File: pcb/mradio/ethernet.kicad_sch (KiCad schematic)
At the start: 28 parts, among them J1 JX0026D21BNL, U2 DP83825I, Y301 DSC1525JL2A-25M00000T

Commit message: ethernet oscillator
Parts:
- added C301: 0.01uF, symbol Device:C_Small
- added Q301: DN2540N3-G, Package_TO_SOT_THT:TO-92_Inline, symbol Transistor_FET_Other:DN2540N3-G
- renumbered C301 to C302, C4 to C303, C3 to C304, C2 to C305, C1 to C306, C8 to C307, C7 to C308, C6 to C309, C5 to C310, C313 to C311, C314 to C312, FB1 to FB301, FB2 to FB302, J1 to J301, R1 to R302, TP302 to TP301, TP303 to TP302, TP4 to TP303, TP3 to TP304, TP1 to TP305, TP2 to TP306, TP301 to TP307, U2 to U301
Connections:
- net +1V8: now also C302.1, Y301.4 (Vcc)
- net ETH_MDIO: now also U301.15 (MDIO)
- net ETH_RESET: now also Q301.2 (G); no longer TP302.1, U301.5 (~{RST})
- net GND: now also Y301.2 (GND), C301.2
- net at R302.2: now also Y301.1 (OE)
- net at TP301.1, U301.13 (XI/50MHzIn): now also Y301.3 (OUT)
- net at R301.1: now also Q301.1 (S)
- new net: C301.1, Q301.3 (D), TP302.1, U301.5 (~{RST})
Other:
- moved on the sheet: C302, R303, Y301

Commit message: Fixed numbers
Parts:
- removed C301: 0.01uF, symbol Device:C_Small
- removed C312: 0.1uF, symbol Device:C_Small
- removed J301: JX0026D21BNL, JX0026D21BNL:JX0026D21BNL, symbol symbols:JX0026D21BNL
- removed Q301: DN2540N3-G, Package_TO_SOT_THT:TO-92_Inline, symbol Transistor_FET_Other:DN2540N3-G
- removed R301: 2.2k, Package_TO_SOT_THT:TO-92_Inline, symbol Device:R
- removed R302: 70k, symbol Device:R_Small
- removed R305: R, symbol Device:R
- removed TP301, TP302, TP303, TP304, TP305, TP306, TP307: TestPoint, symbol Connector:TestPoint
- added C309: 0.1uF, symbol Device:C_Small
- added J301: RJ45_Wuerth_7499010211A, Connector_RJ:RJ45_Wuerth_7499010211A_Horizontal, symbol Connector:RJ45_Wuerth_7499010211A
- added R303: R, symbol Device:R
- R301: renamed from R303; value 2.2k -> (none)
- renumbered C302 to C301, C303 to C302, C304 to C303, C305 to C304, C306 to C305, C307 to C306, C308 to C307, C309 to C308, R304 to R302
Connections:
- net +1V8: now also Y301.1 (OE)
- net ETH_LINK: now also R303.2
- net ETH_RESET: now also U301.5 (~{RST})
- net GND: now also C309.2, J301.10, J301.11, J301.12
- net at U301.11 (TD+): now also J301.1 (TD+)
- net at U301.10 (TD-): now also J301.2 (TD-)
- net at C311.2: now also J301.4 (CTD)
- net at U301.8 (RD+): now also J301.3 (RD+)
- net at U301.7 (RD-): now also J301.6 (RD-)
- new net: C309.1, J301.5 (CRD)
- new net: J301.9, R303.1
- new net GNDPWR: J301.SH
- no-connect marks 6 -> 2
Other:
- moved on the sheet: C301, R301, R302, Y301

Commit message: undid overwrite
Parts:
- removed C309: 0.1uF, symbol Device:C_Small
- removed J301: RJ45_Wuerth_7499010211A, Connector_RJ:RJ45_Wuerth_7499010211A_Horizontal, symbol Connector:RJ45_Wuerth_7499010211A
- removed R303: R, symbol Device:R
- added C301: 0.01uF, symbol Device:C_Small
- added C312: 0.1uF, symbol Device:C_Small
- added J301: JX0026D21BNL, JX0026D21BNL:JX0026D21BNL, symbol symbols:JX0026D21BNL
- added Q301: DN2540N3-G, Package_TO_SOT_THT:TO-92_Inline, symbol Transistor_FET_Other:DN2540N3-G
- added R301: 2.2k, Package_TO_SOT_THT:TO-92_Inline, symbol Device:R
- added R302: 70k, symbol Device:R_Small
- added R305: R, symbol Device:R
- added TP301, TP302, TP303, TP304, TP305, TP306, TP307: TestPoint, symbol Connector:TestPoint
- R303: renamed from R301; value (none) -> 2.2k
- renumbered C301 to C302, C302 to C303, C303 to C304, C304 to C305, C305 to C306, C306 to C307, C307 to C308, C308 to C309, R302 to R304
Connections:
- net +1V8: now also R302.1; no longer Y301.1 (OE)
- net ETH_LINK: now also R305.2
- net ETH_RESET: now also Q301.2 (G); no longer U301.5 (~{RST})
- net ETH_RXD0: now also TP303.1
- net ETH_RXD1: now also TP304.1
- net ETH_TXD0: now also TP305.1
- net ETH_TXD1: now also TP306.1
- net GND: now also C301.2, C312.1, J301.12 (A_GREEN), J301.4 (CHS_GROUND_1), J301.5 (CHS_GROUND_2), R301.2
- net at U301.11 (TD+): now also J301.1 (TD+)
- net at U301.10 (TD-): now also J301.2 (TD-)
- net at U301.8 (RD+): now also J301.7 (RD+)
- net at C311.2: now also J301.3 (CT_1)
- net at U301.7 (RD-): now also J301.8 (RD-)
- net at U301.13 (XI/50MHzIn), Y301.3 (OUT): now also TP301.1
- net at R304.1, U301.14 (RBIAS): now also TP307.1
- new net: Q301.1 (S), R301.1
- new net: C301.1, Q301.3 (D), TP302.1, U301.5 (~{RST})
- new net: R302.2, Y301.1 (OE)
- new net: J301.11 (K_GREEN), R305.1
- new net: C312.2, J301.6 (CT_2)
- no-connect marks 2 -> 6
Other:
- moved on the sheet: C302, R303, R304, Y301

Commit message: ethernet erc
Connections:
- net ETH_LINK: now also U301.16 (MDC); no longer U301.4 (LED0/S(ANEG_Dis))
- net ETH_MDC: now also U301.4 (LED0/S(ANEG_Dis)); no longer U301.16 (MDC)

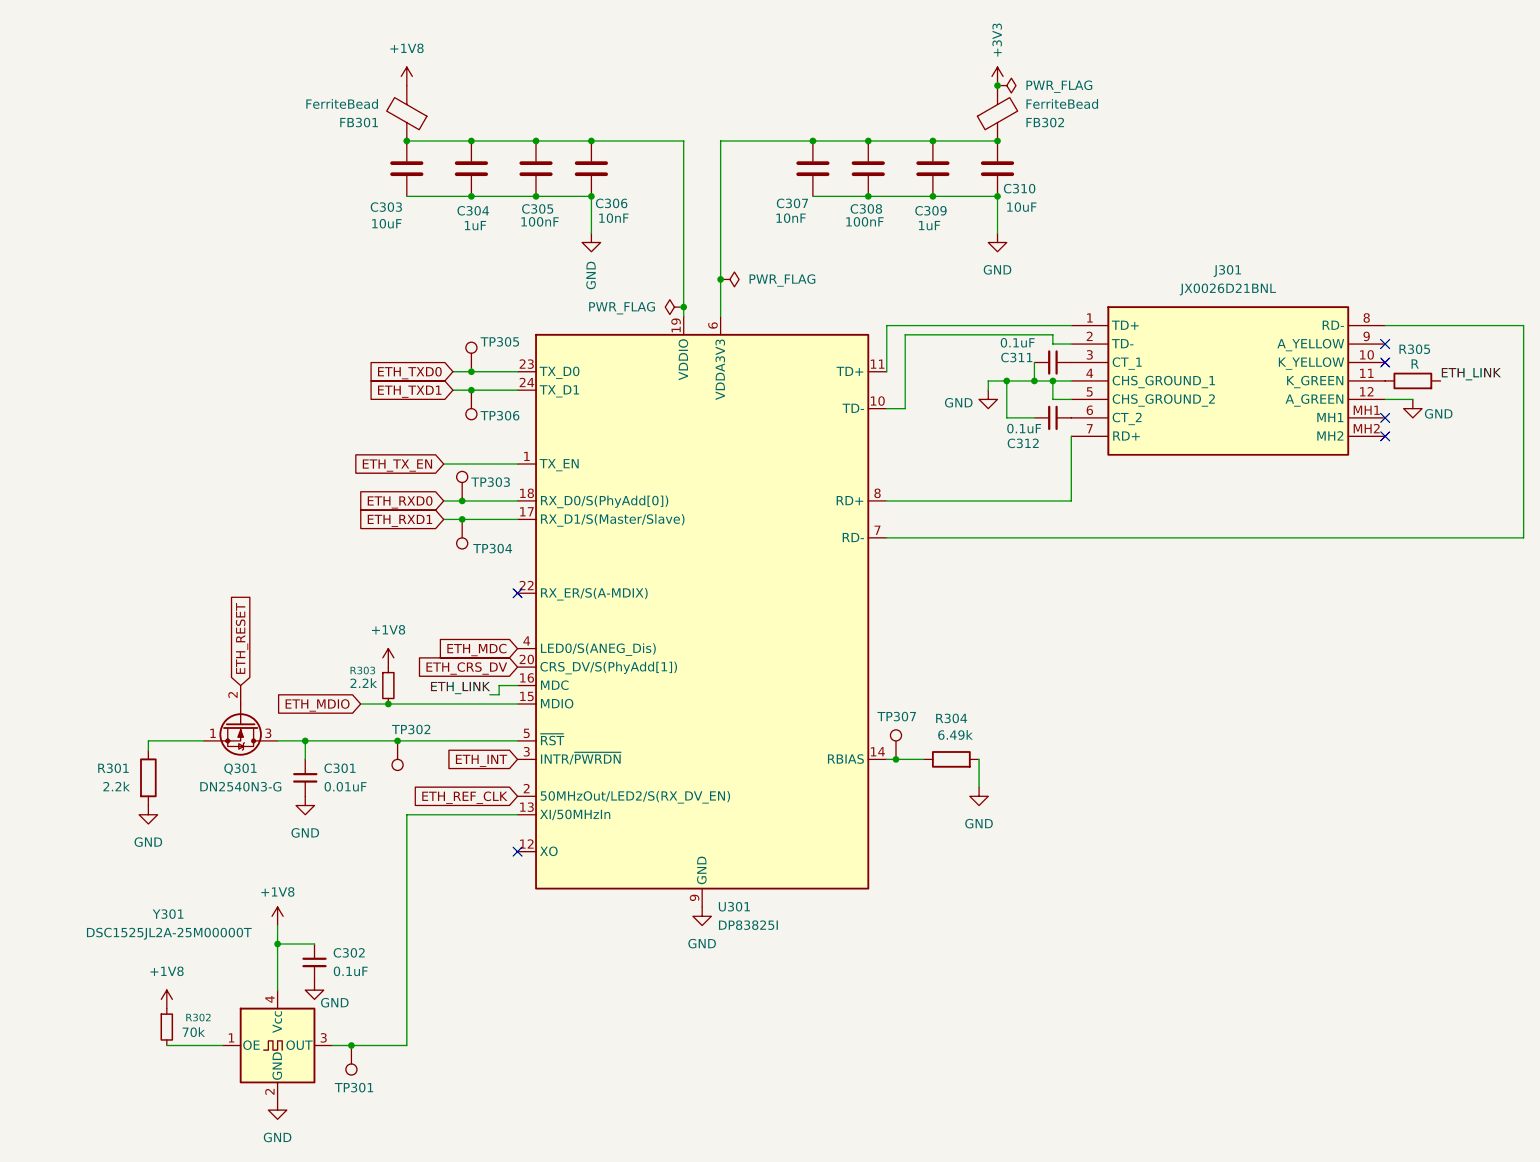
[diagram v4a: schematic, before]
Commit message: changed eth mosfet
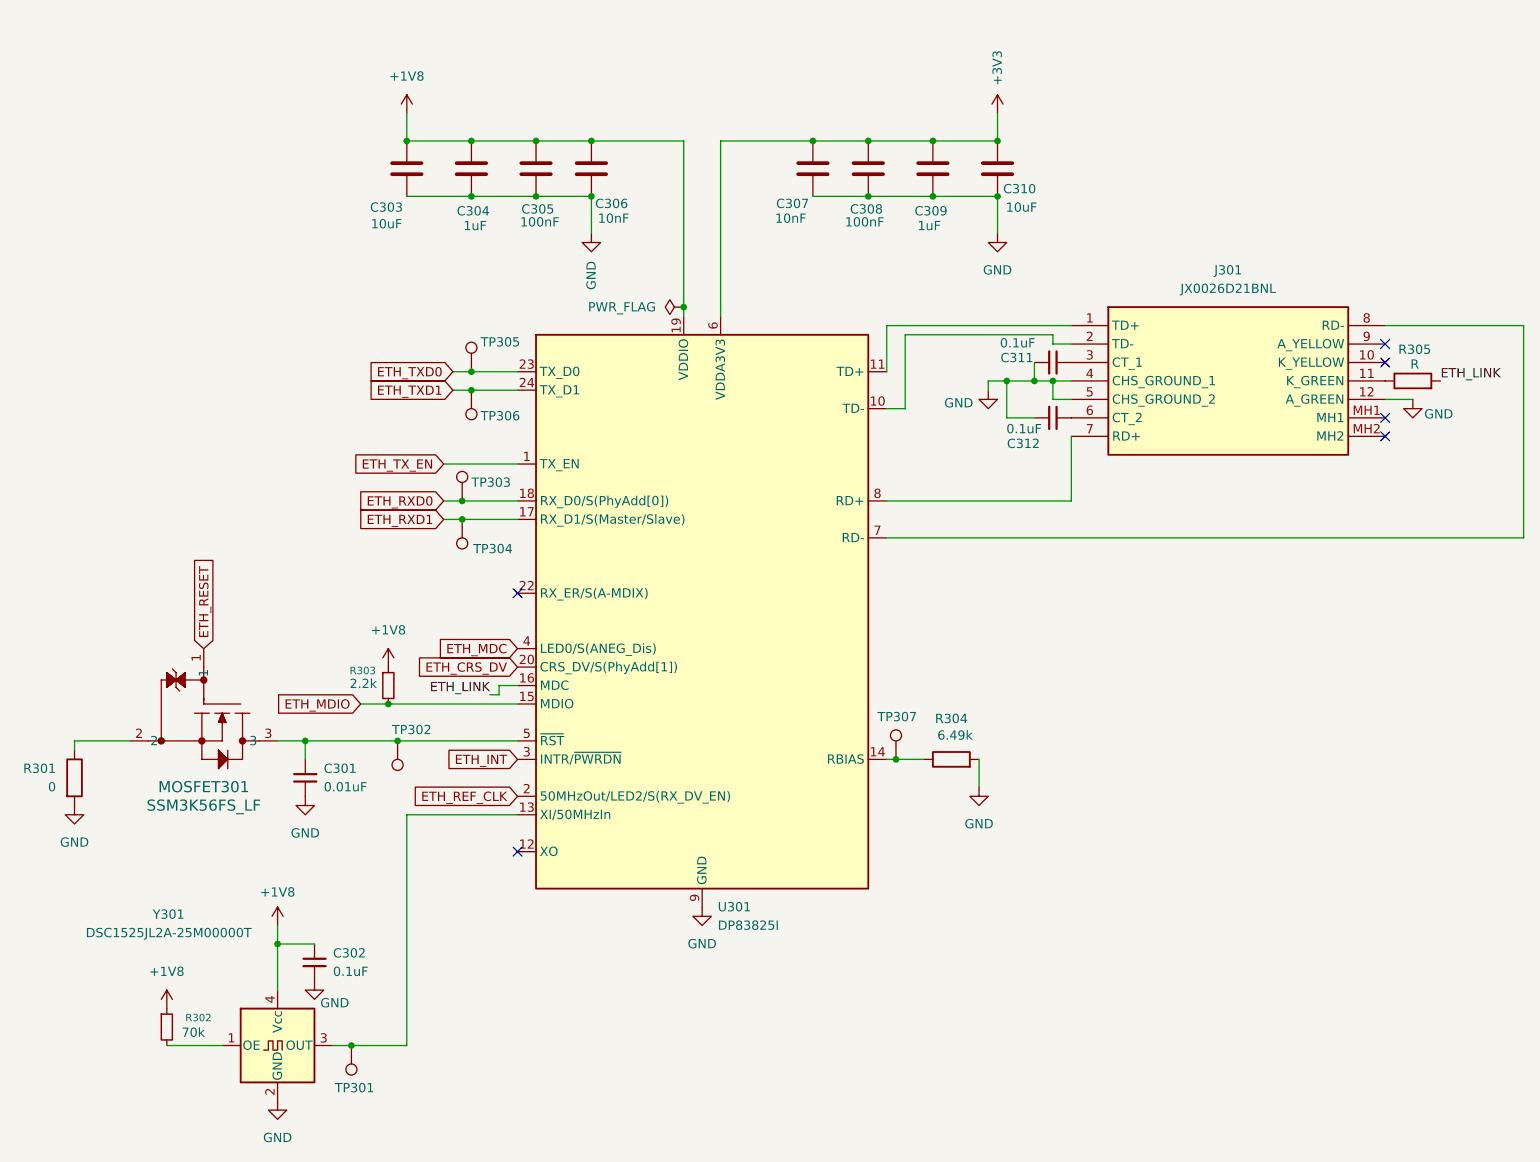
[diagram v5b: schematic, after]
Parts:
- removed FB301, FB302: FerriteBead, Package_LCC:PLCC-84_29.3x29.3mm_P1.27mm, symbol Device:FerriteBead
- removed Q301: DN2540N3-G, Package_TO_SOT_THT:TO-92_Inline, symbol Transistor_FET_Other:DN2540N3-G
- added MOSFET301: SSM3K56FS_LF, SSM3K56FS:SSM_TOS, symbol symbols:SSM3K56FS_LF
- C301, C302, C303, C304, C305, C308, C309, C310, C311, C312: footprint (none) -> Capacitor_SMD:C_0603_1608Metric
- C306, C307: footprint Package_SO:SOIC-8_3.9x4.9mm_P1.27mm -> Capacitor_SMD:C_0603_1608Metric
- R301: value 2.2k -> 0; footprint Package_TO_SOT_THT:TO-92_Inline -> Resistor_SMD:R_0603_1608Metric
- R302, R303, R304, R305: footprint (none) -> Resistor_SMD:R_0603_1608Metric
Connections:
- net +1V8: now also C303.2, C304.2, C305.2, C306.2, U301.19 (VDDIO)
- net +3V3: now also C307.2, C308.2, C309.2, C310.2, U301.6 (VDDA3V3)
- net ETH_RESET: now also MOSFET301.1
- net at R301.1: now also MOSFET301.2
- net at C301.1, TP302.1, U301.5 (~{RST}): now also MOSFET301.3
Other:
- moved on the sheet: R301

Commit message: Update some footprints
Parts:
- TP301, TP302, TP303, TP304, TP305, TP306, TP307: footprint (none) -> TestPoint:TestPoint_Loop_D2.60mm_Drill0.9mm_Beaded
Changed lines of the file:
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@@
 			)
 		)
-		(property "Footprint" ""
+		(property "Footprint" "TestPoint:TestPoint_Loop_D2.60mm_Drill0.9mm_Beaded"
 			(at 90.17 171.45 0)
 			(hide yes)
@@
 			)
 		)
-		(property "Footprint" ""
+		(property "Footprint" "TestPoint:TestPoint_Loop_D2.60mm_Drill0.9mm_Beaded"
 			(at 115.57 96.52 0)
 			(hide yes)
@@
 			)
 		)
-		(property "Footprint" ""
+		(property "Footprint" "TestPoint:TestPoint_Loop_D2.60mm_Drill0.9mm_Beaded"
 			(at 106.68 81.28 0)
 			(hide yes)
@@
 			)
 		)
-		(property "Footprint" ""
+		(property "Footprint" "TestPoint:TestPoint_Loop_D2.60mm_Drill0.9mm_Beaded"
 			(at 116.84 78.74 0)
 			(hide yes)
@@
 			)
 		)
-		(property "Footprint" ""
+		(property "Footprint" "TestPoint:TestPoint_Loop_D2.60mm_Drill0.9mm_Beaded"
 			(at 175.26 132.08 0)
 			(hide yes)
@@
 			)
 		)
-		(property "Footprint" ""
+		(property "Footprint" "TestPoint:TestPoint_Loop_D2.60mm_Drill0.9mm_Beaded"
 			(at 105.41 99.06 0)
 			(hide yes)
@@
 			)
 		)
-		(property "Footprint" ""
+		(property "Footprint" "TestPoint:TestPoint_Loop_D2.60mm_Drill0.9mm_Beaded"
 			(at 96.52 129.54 0)
 			(hide yes)

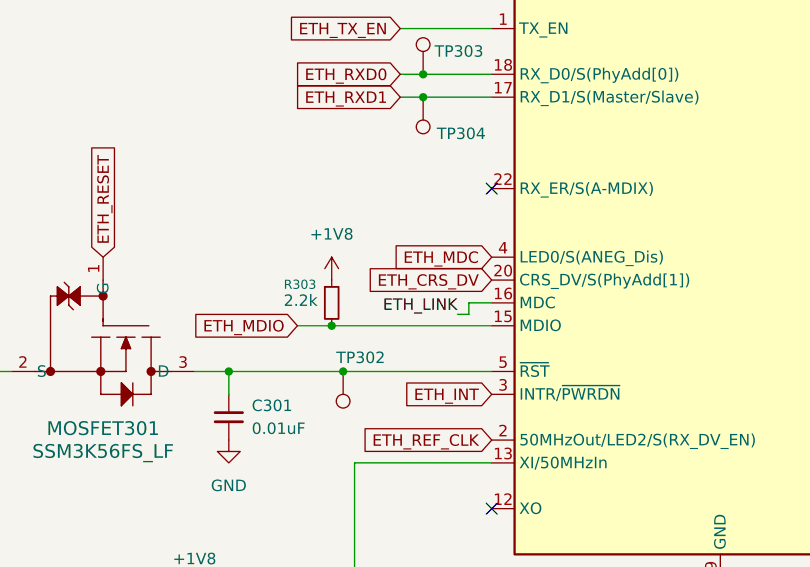
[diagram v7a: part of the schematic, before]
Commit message: fixed eth lines
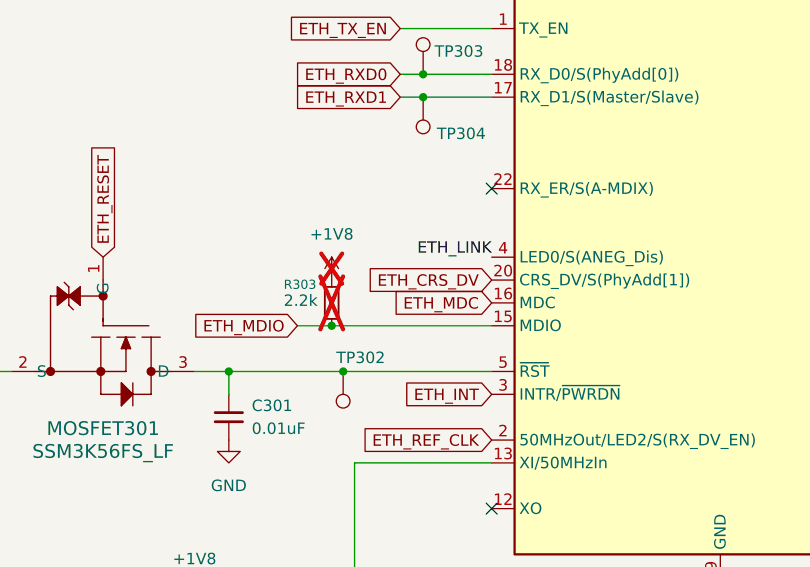
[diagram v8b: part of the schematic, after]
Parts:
- R303: now not fitted
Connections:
- net ETH_LINK: now also U301.4 (LED0/S(ANEG_Dis)); no longer U301.16 (MDC)
- net ETH_MDC: now also U301.16 (MDC); no longer U301.4 (LED0/S(ANEG_Dis))
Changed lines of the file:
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@@
 	(wire
 		(pts
-			(xy 115.57 123.19) (xy 115.57 121.92)
-		)
-		(stroke
-			(width 0)
-			(type default)
-		)
-	)
-	(wire
-		(pts
 			(xy 191.77 74.93) (xy 191.77 73.66)
 		)
@@
 	(wire
 		(pts
-			(xy 115.57 121.92) (xy 118.11 121.92)
-		)
-		(stroke
-			(width 0)
-			(type default)
-		)
-	)
-	(wire
-		(pts
 			(xy 168.91 96.52) (xy 194.31 96.52)
 		)
@@
 	(wire
 		(pts
-			(xy 114.3 123.19) (xy 115.57 123.19)
-		)
-		(stroke
-			(width 0)
-			(type default)
-		)
-	)
-	(wire
-		(pts
 			(xy 171.45 83.82) (xy 168.91 83.82)
 		)
@@
 	)
 	(label "ETH_LINK"
-		(at 114.3 123.19 180)
+		(at 118.11 116.84 180)
 		(effects
 			(font
@@
 		)
 	)
-	(global_label "ETH_MDC"
+	(global_label "ETH_TXD0"
 		(shape input)
-		(at 118.11 116.84 180)
+		(at 109.22 78.74 180)
 		(fields_autoplaced yes)
 		(effects
@@
 		)
 		(property "Intersheetrefs" "${INTERSHEET_REFS}"
-			(at 106.7187 116.84 0)
+			(at 97.1635 78.74 0)
 			(hide yes)
 			(show_name no)
@@
 		)
 	)
-	(global_label "ETH_TXD0"
+	(global_label "ETH_TX_EN"
 		(shape input)
-		(at 109.22 78.74 180)
+		(at 107.95 91.44 180)
 		(fields_autoplaced yes)
 		(effects
@@
 		)
 		(property "Intersheetrefs" "${INTERSHEET_REFS}"
-			(at 97.1635 78.74 0)
+			(at 94.9259 91.44 0)
 			(hide yes)
 			(show_name no)
@@
 		)
 	)
-	(global_label "ETH_TX_EN"
+	(global_label "ETH_MDC"
 		(shape input)
-		(at 107.95 91.44 180)
+		(at 118.11 121.92 180)
 		(fields_autoplaced yes)
 		(effects
@@
 		)
 		(property "Intersheetrefs" "${INTERSHEET_REFS}"
-			(at 94.9259 91.44 0)
+			(at 106.7187 121.92 0)
 			(hide yes)
 			(show_name no)
@@
 		(on_board yes)
 		(in_pos_files yes)
-		(dnp no)
+		(dnp yes)
 		(property "Reference" "R303"
 			(at 94.996 119.888 0)
@@
 		(on_board yes)
 		(in_pos_files yes)
-		(dnp no)
+		(dnp yes)
 		(fields_autoplaced yes)
 		(property "Reference" "#PWR0307"
